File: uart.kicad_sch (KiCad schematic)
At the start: 45 parts, among them J17 USB_B, J18 D09P33E4GV00LF, J19 D09P33E4GV00LF, U17 TS5A23159DGS, U18 CP2104, U19 TRS3221ECPW, U20 TRS3221ECPW

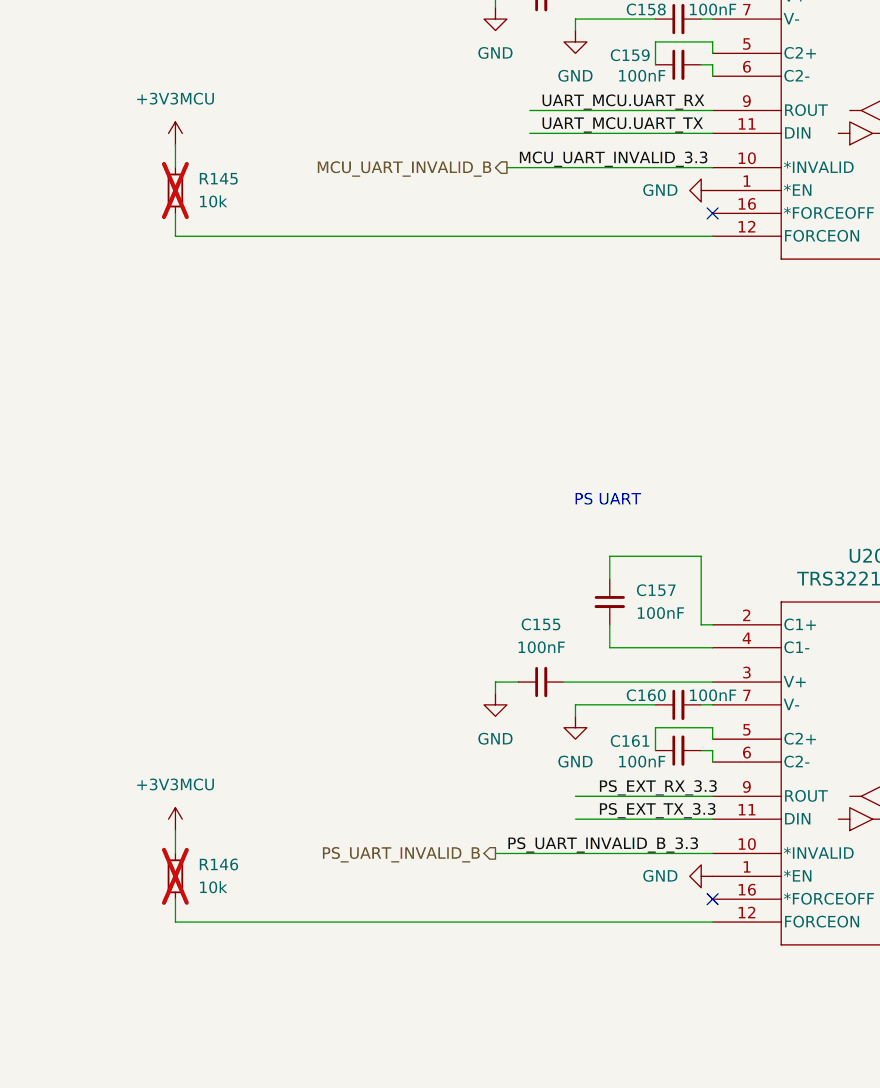
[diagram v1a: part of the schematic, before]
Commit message: schema: uart transceivers are forced on correctly
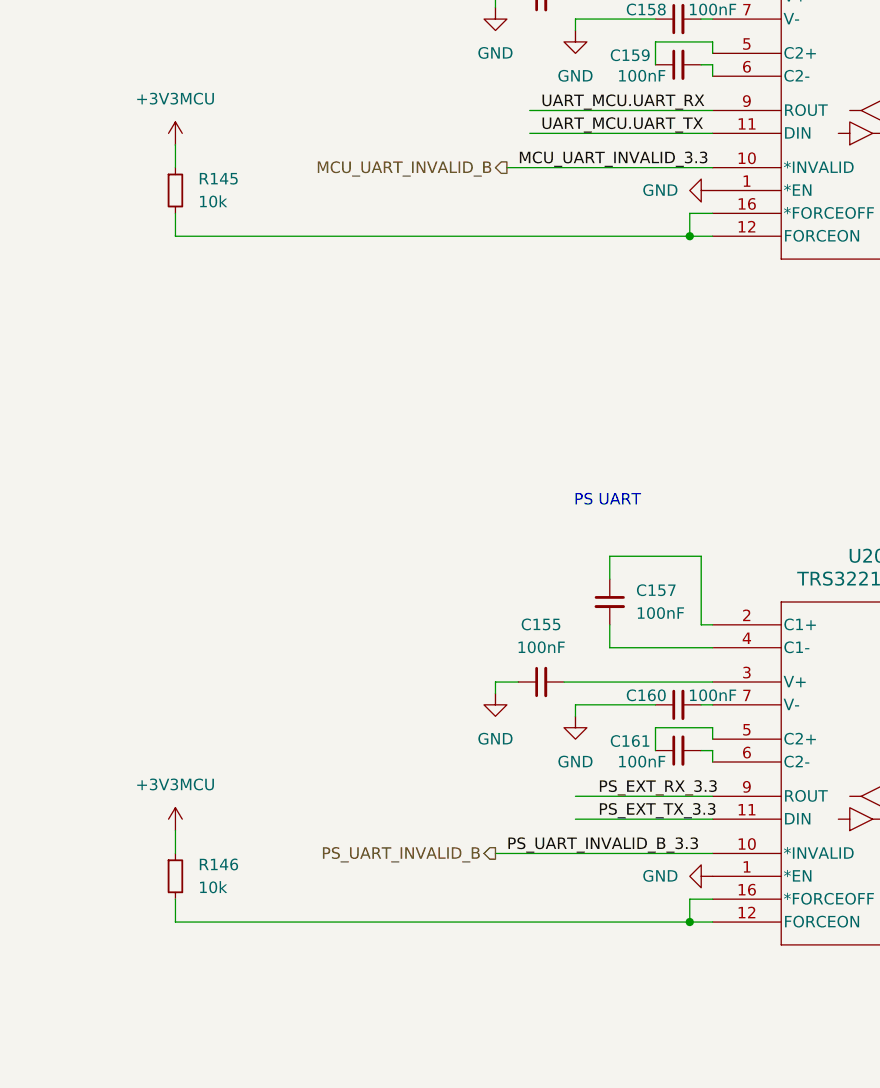
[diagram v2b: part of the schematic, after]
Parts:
- R145, R146: now fitted
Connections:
- net at R146.2, U20.12 (FORCEON): now also U20.16 (*FORCEOFF)
- net at R145.2, U19.12 (FORCEON): now also U19.16 (*FORCEOFF)
- no-connect marks 25 -> 23
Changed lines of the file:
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@@
 	)
 	(junction
+		(at 307.34 149.86)
+		(diameter 0)
+		(color 0 0 0 0)
+	)
+	(junction
 		(at 90.17 22.86)
 		(diameter 0)
@@
 	)
 	(junction
+		(at 307.34 73.66)
+		(diameter 0)
+		(color 0 0 0 0)
+	)
+	(junction
 		(at 34.29 238.76)
 		(diameter 0)
@@
 	)
 	(no_connect
-		(at 309.88 71.12)
-	)
-	(no_connect
 		(at 100.33 83.82)
 	)
@@
 	)
 	(no_connect
-		(at 309.88 147.32)
-	)
-	(no_connect
 		(at 100.33 58.42)
 	)
@@
 	(wire
 		(pts
+			(xy 307.34 149.86) (xy 309.88 149.86)
+		)
+		(stroke
+			(width 0)
+			(type default)
+		)
+	)
+	(wire
+		(pts
 			(xy 82.55 219.71) (xy 107.95 219.71)
 		)
@@
 	(wire
 		(pts
+			(xy 307.34 147.32) (xy 309.88 147.32)
+		)
+		(stroke
+			(width 0)
+			(type default)
+		)
+	)
+	(wire
+		(pts
 			(xy 308.61 130.81) (xy 309.88 130.81)
 		)
@@
 	(wire
 		(pts
+			(xy 307.34 149.86) (xy 307.34 147.32)
+		)
+		(stroke
+			(width 0)
+			(type default)
+		)
+	)
+	(wire
+		(pts
 			(xy 36.83 68.58) (xy 43.18 68.58)
 		)
@@
 	(wire
 		(pts
+			(xy 309.88 71.12) (xy 307.34 71.12)
+		)
+		(stroke
+			(width 0)
+			(type default)
+		)
+	)
+	(wire
+		(pts
 			(xy 54.61 60.96) (xy 54.61 76.2)
 		)
@@
 	(wire
 		(pts
+			(xy 307.34 73.66) (xy 309.88 73.66)
+		)
+		(stroke
+			(width 0)
+			(type default)
+		)
+	)
+	(wire
+		(pts
 			(xy 307.34 33.02) (xy 298.45 33.02)
 		)
@@
 	(wire
 		(pts
+			(xy 307.34 71.12) (xy 307.34 73.66)
+		)
+		(stroke
+			(width 0)
+			(type default)
+		)
+	)
+	(wire
+		(pts
 			(xy 97.79 209.55) (xy 116.84 209.55)
 		)
@@
 	(wire
 		(pts
-			(xy 250.19 73.66) (xy 309.88 73.66)
+			(xy 250.19 73.66) (xy 307.34 73.66)
 		)
 		(stroke
@@
 	(wire
 		(pts
-			(xy 250.19 149.86) (xy 309.88 149.86)
+			(xy 250.19 149.86) (xy 307.34 149.86)
 		)
 		(stroke
@@
 		(in_bom yes)
 		(on_board yes)
-		(dnp yes)
+		(dnp no)
 		(fields_autoplaced yes)
 		(property "Reference" "R146"
@@
 		(in_bom yes)
 		(on_board yes)
-		(dnp yes)
+		(dnp no)
 		(fields_autoplaced yes)
 		(property "Reference" "R145"
